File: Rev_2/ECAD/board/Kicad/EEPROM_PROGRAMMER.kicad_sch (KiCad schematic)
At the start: 37 parts, among them Q1 PMOS, Q2 PNP, Q3 PNP, Q4 NPN, U1 FT232RL, U2 ATMega328P-AU, U3 ICSP, U4 SD_CARD_READER, U5 SUM, Y1 16MHz

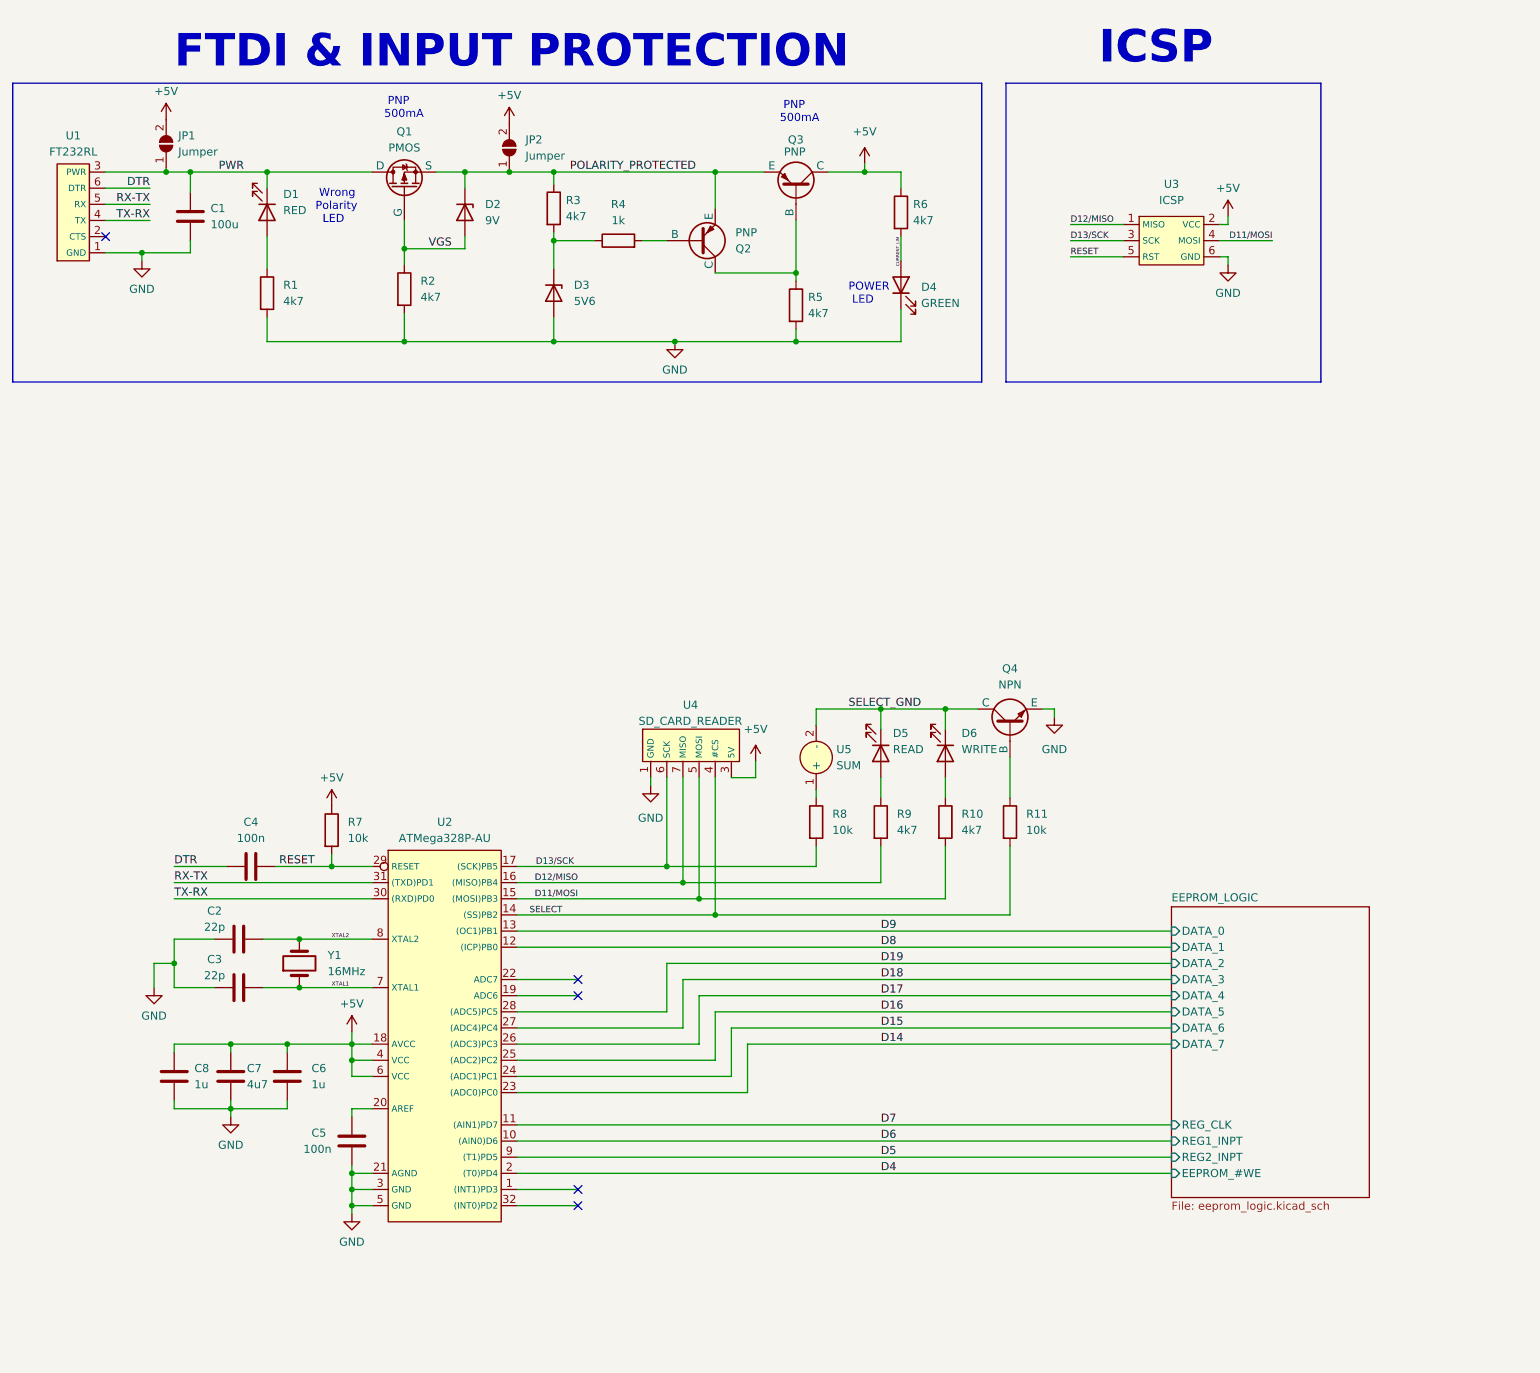
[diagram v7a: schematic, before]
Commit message: Added Bypass capacitors aswell as pullup resistors
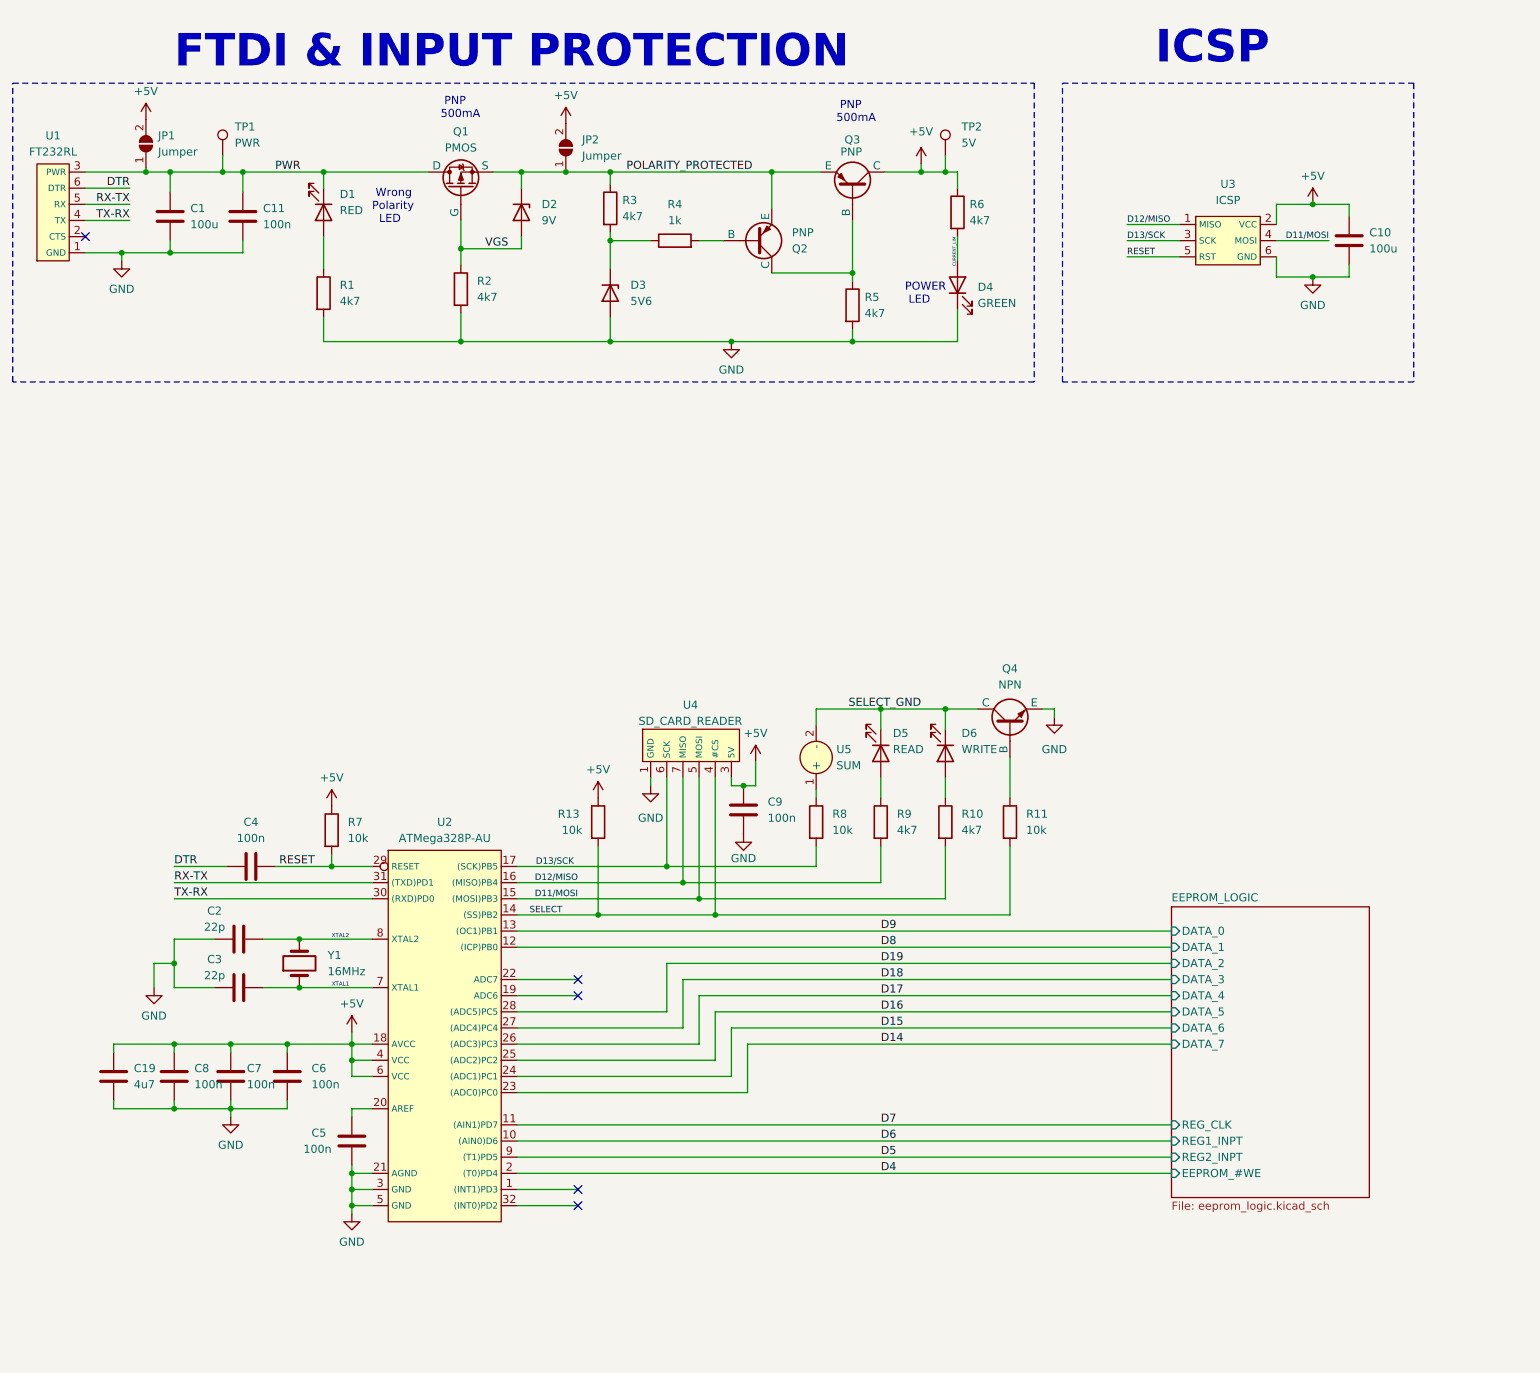
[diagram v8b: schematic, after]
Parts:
- added C10: 100u, Capacitor_THT:CP_Radial_D6.3mm_P2.50mm, symbol Device:C
- added C11, C9: 100n, Capacitor_THT:CP_Radial_D6.3mm_P2.50mm, symbol Device:C
- added C19: 4u7, Capacitor_THT:CP_Radial_D6.3mm_P2.50mm, symbol Device:C
- added R13: 10k, Resistor_SMD:R_0805_2012Metric_Pad1.20x1.40mm_HandSolder, symbol Device:R
- added TP1: PWR, symbol Connector:TestPoint
- added TP2: 5V, symbol Connector:TestPoint
- C6, C8: value 1u -> 100n
- C7: value 4u7 -> 100n
- D2, D3: footprint (none) -> Diode_THT:D_DO-35_SOD27_P3.81mm_Vertical_AnodeUp
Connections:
- net +5V: now also C10.1, C19.2, C9.2, R13.1, TP2.1
- net GND: now also C10.2, C11.2, C19.1, C9.1
- net PWR: now also C11.1, TP1.1
- net SELECT: now also R13.2
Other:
- moved on the sheet: C1, D1, D2, D3, D4, JP1, JP2, Q1, Q2, Q3, R1, R2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
